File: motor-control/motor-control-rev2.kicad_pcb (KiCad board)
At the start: 2 copper layers, 155.7 x 66 mm, 79 parts, among them P1 CONN_02X12, P2 to_motor_phase_1, P3 to_motor_phase_2, P4 to_motor_phase_3, P5 CONN_01X01, P6 CONN_01X01, P7 CONN_01X04, Q1 csd19505kcs, Q10 csd19505kcs, Q11 csd19505kcs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

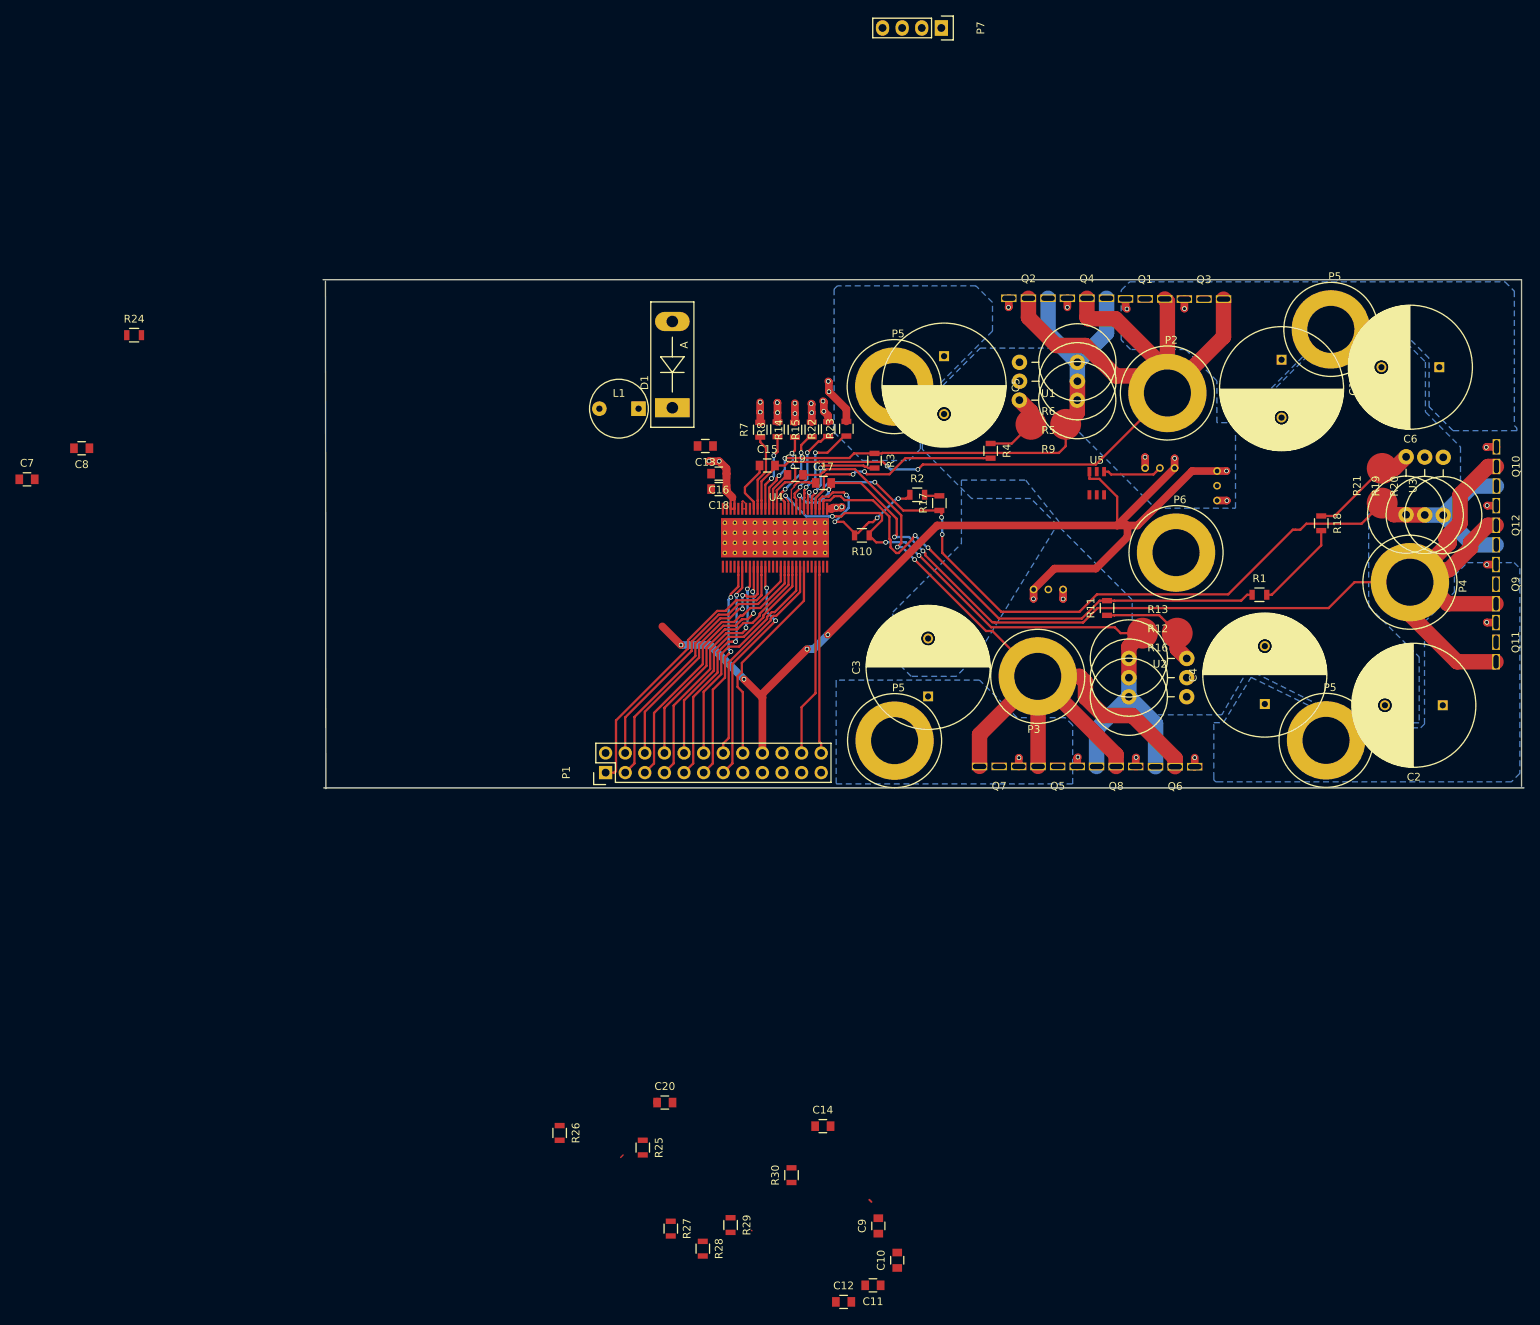
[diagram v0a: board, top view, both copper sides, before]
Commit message: Moved in all components, need last traces and GND
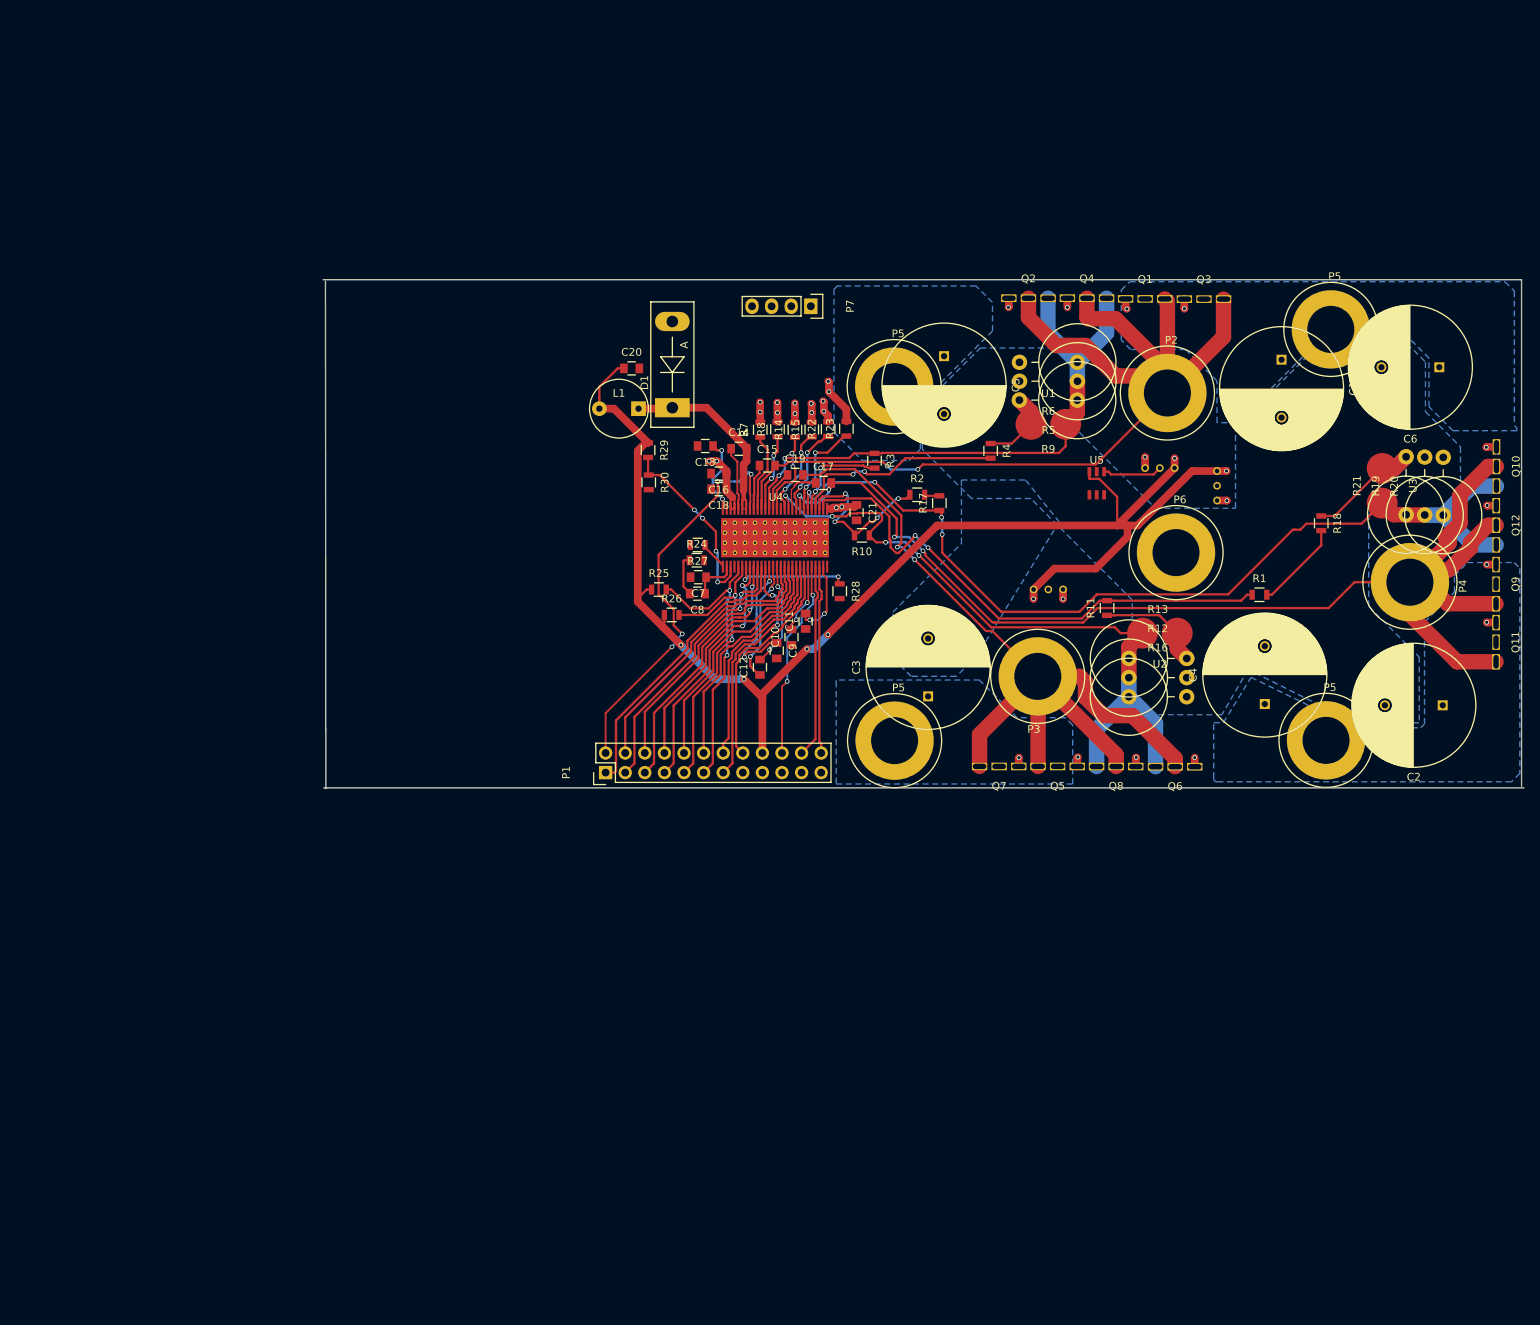
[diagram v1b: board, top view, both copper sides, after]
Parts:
- added C21: C_Small, Capacitors_SMD:C_0805, F.Cu at (110.8, 53.7)
- moved R29 101.0 mm to (83.7, 45.6)
- moved C20 95.2 mm to (81.6, 35.1)
- moved R30 91.7 mm to (83.8, 49.8), turned to 270 degrees
- moved R27 88.7 mm to (90.2, 57.9), turned to 180 degrees
- moved C14 88.5 mm to (95.5, 45.5)
- moved C7 87.9 mm to (90.2, 62.1), turned to 180 degrees
- moved R28 87.0 mm to (108.6, 63.9)
- moved C11 86.5 mm to (104.2, 67.8), turned to 90 degrees
- moved C12 83.0 mm to (98.2, 73.8), turned to 90 degrees
- moved C8 82.0 mm to (90.1, 64.2)
- moved C10 81.9 mm to (102.3, 69.9)
- moved R24 78.5 mm to (90.0, 59.9)
- moved C9 75.7 mm to (100.4, 71.6), turned to 270 degrees
- moved R25 72.4 mm to (85.1, 63.7), turned to 0 degrees
- moved R26 68.7 mm to (86.8, 67.0), turned to 0 degrees
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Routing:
- net /Gate-Driver/VDD_SPI: track 0.00 -> 53.3 mm, vias 0 -> 4
- net VCC: track 135.4 -> 180.6 mm
- net Net-(C14-Pad2): track 2.86 -> 29.7 mm
- net /Gate-Driver/REF: track 0.00 -> 25.9 mm, vias 0 -> 2
- net Net-(R29-Pad2): track 0.00 -> 23.9 mm, vias 0 -> 4
- net Net-(C9-Pad1): track 0.00 -> 18.2 mm, vias 0 -> 2
- net Net-(C12-Pad1): track 0.00 -> 16.0 mm, vias 0 -> 2
- net Net-(R28-Pad1): track 0.00 -> 15.0 mm, vias 0 -> 2
- net Net-(C12-Pad2): track 0.00 -> 13.6 mm, vias 0 -> 2
- net Net-(C13-Pad1): track 0.00 -> 9.96 mm, vias 0 -> 2
- net Net-(C11-Pad2): track 0.00 -> 9.96 mm, vias 0 -> 2
- net /Gate-Driver/nOCTW: track 28.8 -> 38.8 mm
- net Net-(C10-Pad2): track 0.00 -> 9.06 mm, vias 0 -> 2
- net Net-(C14-Pad1): track 0.12 -> 9.02 mm
- net /Gate-Driver/nFault: track 30.4 -> 38.3 mm
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
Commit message: All components in place, now to fix it up
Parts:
- moved P7 56.2 mm to (158.1, 45.0)
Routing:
- net /power mosfets & current sensing/hall_3: track 1.28 -> 76.6 mm, vias 1 -> 5
- net /power mosfets & current sensing/hall_2: track 1.41 -> 72.6 mm, vias 1 -> 4
- net /power mosfets & current sensing/hall_1: track 1.24 -> 51.4 mm, vias 1 -> 5
- net GND: track 45.8 -> 71.8 mm
- net Net-(P7-Pad1): track 0.00 -> 18.0 mm, vias 0 -> 1
- net Net-(P7-Pad2): track 0.00 -> 18.0 mm, vias 0 -> 1
- net Net-(P7-Pad3): track 0.00 -> 17.5 mm, vias 0 -> 1
- net Net-(P7-Pad4): track 0.00 -> 10.3 mm
- net /Gate-Driver/SL_C: track 119.4 -> 118.3 mm
- net VCC: track 180.6 -> 179.6 mm

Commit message: Stuff I didn't commit from last time
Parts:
- moved C6 2.48 mm to (188.8, 35.1)
- moved C1 0.62 mm to (165.2, 33.9)
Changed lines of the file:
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@@
     (links 228)
     (no_connects 38)
-    (area 41.530199 23.483499 197.331401 89.584601)
+    (area 41.530199 20.5104 197.331401 92.527833)
     (thickness 1.6)
     (drawings 5)
@@
       (padsonsilk false)
       (subtractmaskfromsilk false)
-      (outputformat 4)
+      (outputformat 1)
       (mirror false)
-      (drillshape 2)
+      (drillshape 0)
       (scaleselection 1)
       (outputdirectory "C:/Users/terminator/Documents/classwork/senior design/plots/"))
@@
   )
   (module Capacitors_ThroughHole:C_Radial_D16_L30_P7.5 (layer F.Cu)
-    (at 165.8366 33.9274 270)
+    (at 165.2143 33.9344 270)
     (descr "Radial Electrolytic Capacitor Diameter 16mm x Length 25mm, Pitch 7.5mm")
     (tags "Electrolytic Capacitor")
@@
   )
   (module Capacitors_ThroughHole:C_Radial_D16_L30_P7.5 (layer F.Cu)
-    (at 186.2836 34.8996 180)
+    (at 188.7601 35.052 180)
     (descr "Radial Electrolytic Capacitor Diameter 16mm x Length 25mm, Pitch 7.5mm")
     (tags "Electrolytic Capacitor")
@@
     (polygon
       (pts
-        (xy 183.6674 80.9879) (xy 175.3362 80.9879) (xy 161.5059 74.0791) (xy 158.0896 79.9465) (xy 146.4818 79.9465)
+        (xy 182.9689 80.3148) (xy 177.546 79.7941) (xy 161.3662 73.0504) (xy 157.1879 79.502) (xy 146.4818 79.9465)
         (xy 146.4818 65.0621) (xy 133.3373 51.9176) (xy 125.6665 51.9176) (xy 119.2784 45.5295) (xy 119.2784 39.9288)
         (xy 126.7841 32.4231) (xy 138.7475 32.4231) (xy 138.7475 42.4561) (xy 149.4663 53.1749) (xy 159.8676 53.1749)
-        (xy 159.8676 42.7736) (xy 172.5803 30.0609) (xy 180.3273 30.0609) (xy 184.4802 34.2138) (xy 184.4802 40.6781)
-        (xy 189.0268 45.2247) (xy 189.0268 53.9242) (xy 177.1269 53.9242) (xy 177.1269 65.9003) (xy 183.6674 72.4408)
+        (xy 160.5407 42.9006) (xy 168.4909 34.7218) (xy 169.6974 35.6235) (xy 174.6885 35.2171) (xy 177.5968 32.4739)
+        (xy 177.9651 30.1625) (xy 180.8861 30.2006) (xy 184.4802 34.2138) (xy 184.4802 40.6781) (xy 189.0268 45.2247)
+        (xy 189.0268 53.9242) (xy 177.1269 53.9242) (xy 177.1269 65.9003) (xy 183.1213 72.4154)
       )
     )

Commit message: Added bottom solder mask layer
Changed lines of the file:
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@@
-    (polygon
-      (pts
-        (xy 157.0482 88.1507) (xy 157.0482 80.9752) (xy 158.2928 80.9752) (xy 161.8869 75.0951) (xy 169.9133 79.0067)
-        (xy 173.8884 79.0067) (xy 176.5173 81.6356) (xy 183.8706 81.6356) (xy 184.3659 81.1403) (xy 184.3659 67.9323)
-        (xy 188.2394 64.0588) (xy 188.2394 61.8998) (xy 189.9158 60.2234) (xy 195.9864 60.2234) (xy 196.723 60.96)
-        (xy 196.723 87.5411) (xy 195.6308 88.6333) (xy 157.6959 88.6333) (xy 157.3022 88.6333) (xy 157.0482 88.3793)
-      )
-    )
-  )
-  (zone (net 1) (net_name +batt) (layer B.Cu) (hatch edge 0.508)
-    (connect_pads yes (clearance 0.508))
-    (min_thickness 0.254)
-    (fill yes (arc_segments 16) (thermal_gap 0.508) (thermal_bridge_width 0.508))
     (polygon
       (pts
@@
       )
     )
+  )
+  (zone (net 1) (net_name +batt) (layer B.Cu) (hatch edge 0.508)
+    (connect_pads yes (clearance 0.508))
+    (min_thickness 0.254)
+    (fill yes (arc_segments 16) (thermal_gap 0.508) (thermal_bridge_width 0.508))
+    (polygon
+      (pts
+        (xy 156.50718 86.94928) (xy 156.50718 80.3021) (xy 162.56254 74.24674) (xy 166.74084 74.24674) (xy 169.86504 77.37094)
+        (xy 174.1043 77.37094) (xy 178.07178 81.33842) (xy 181.64556 81.33842) (xy 183.47944 79.50454) (xy 183.47944 70.66534)
+        (xy 188.80328 65.3415) (xy 188.80328 62.2681) (xy 190.00724 61.06414) (xy 195.8975 61.06414) (xy 196.40804 61.57468)
+        (xy 196.40804 86.05774) (xy 193.5353 88.93048) (xy 158.4579 88.93048) (xy 156.49956 86.97214)
+      )
+    )
+  )
+  (zone (net 1) (net_name +batt) (layer B.Mask) (hatch edge 0.508)
+    (connect_pads yes (clearance 0.508))
+    (min_thickness 0.254)
+    (fill yes (arc_segments 16) (thermal_gap 0.508) (thermal_bridge_width 0.508))
+    (polygon
+      (pts
+        (xy 183.47944 70.66534) (xy 183.47944 79.44104) (xy 181.62778 81.2927) (xy 178.06924 81.2927) (xy 174.12208 77.34554)
+        (xy 169.88536 77.34554) (xy 166.74846 74.20864) (xy 162.54984 74.20864) (xy 156.47416 80.28432) (xy 156.47416 87.0077)
+        (xy 158.4325 88.96604) (xy 193.53276 88.96604) (xy 196.4436 86.0552) (xy 196.4436 76.7461) (xy 194.27444 74.57694)
+        (xy 192.8241 74.57694) (xy 192.4177 74.17054) (xy 192.4177 69.1261) (xy 191.63538 68.34378) (xy 191.63538 67.564)
+        (xy 192.53962 66.65976) (xy 192.53962 64.5414) (xy 192.96634 64.11468) (xy 194.36588 64.11468) (xy 194.63004 64.37884)
+        (xy 194.63004 74.9046) (xy 196.4436 76.71816) (xy 196.4436 61.56198) (xy 195.88734 61.00572) (xy 195.15836 61.00572)
+        (xy 194.59194 61.57214) (xy 194.59194 61.8109) (xy 192.76314 61.8109) (xy 192.20688 61.25464) (xy 192.01384 61.25464)
+        (xy 189.92596 61.25464) (xy 188.94552 62.23508) (xy 188.94552 65.2907) (xy 183.60898 70.62724) (xy 183.51754 70.62724)
+      )
+    )
+  )
+  (zone (net 1) (net_name +batt) (layer B.Mask) (hatch edge 0.508)
+    (connect_pads yes (clearance 0.508))
+    (min_thickness 0.254)
+    (fill yes (arc_segments 16) (thermal_gap 0.508) (thermal_bridge_width 0.508))
+    (polygon
+      (pts
+        (xy 133.4389 62.23508) (xy 138.19378 62.23508) (xy 147.98294 72.02424) (xy 147.98294 76.7842) (xy 151.15286 79.95412)
+        (xy 155.89504 79.95412) (xy 162.19932 73.64984) (xy 166.85514 73.64984) (xy 170.06316 76.85786) (xy 174.27448 76.85786)
+        (xy 178.23688 80.82026) (xy 181.40426 80.82026) (xy 182.98922 79.2353) (xy 182.98922 70.93712) (xy 180.36032 68.30822)
+        (xy 178.50358 68.30822) (xy 176.12868 65.93332) (xy 176.12868 59.93638) (xy 179.13604 56.92902) (xy 179.13604 52.4891)
+        (xy 180.64734 50.9778) (xy 187.04306 50.9778) (xy 188.99124 49.02962) (xy 188.99124 45.00626) (xy 184.09158 40.1066)
+        (xy 184.09158 33.85312) (xy 180.66512 30.42666) (xy 179.4891 30.42666) (xy 178.78552 31.13024) (xy 178.78552 33.20034)
+        (xy 175.7045 36.28136) (xy 167.28948 36.28136) (xy 160.34766 43.22318) (xy 160.34766 52.54752) (xy 159.42818 53.467)
+        (xy 149.05736 53.467) (xy 137.58926 41.9989) (xy 137.58926 35.02406) (xy 134.42188 31.85668) (xy 127.8509 31.85668)
+        (xy 121.2723 38.43528) (xy 121.2723 39.93134) (xy 119.65178 41.55186) (xy 119.65178 45.76064) (xy 124.5489 50.65776)
+        (xy 124.5489 56.94426) (xy 115.5065 65.98666) (xy 115.5065 72.43318) (xy 117.67058 74.59726) (xy 122.83948 74.59726)
+        (xy 131.953 65.48374) (xy 131.953 62.89802) (xy 132.61594 62.23508)
+      )
+    )
+  )
+  (zone (net 1) (net_name +batt) (layer B.Mask) (hatch edge 0.508)
+    (connect_pads yes (clearance 0.508))
+    (min_thickness 0.254)
+    (fill yes (arc_segments 16) (thermal_gap 0.508) (thermal_bridge_width 0.508))
+    (polygon
+      (pts
+        (xy 108.18114 75.83424) (xy 108.18114 88.64854) (xy 108.27766 88.74506) (xy 123.75642 88.74506) (xy 125.10262 87.39886)
+        (xy 125.10262 85.91042) (xy 125.44552 85.56752) (xy 127.89154 85.56752) (xy 128.2827 85.95868) (xy 128.2827 87.30234)
+        (xy 127.86614 87.7189) (xy 125.42012 87.7189) (xy 125.1077 87.40648) (xy 123.76658 88.7476) (xy 129.18186 88.7476)
+        (xy 130.43916 87.4903) (xy 130.43916 85.73262) (xy 131.47548 84.6963) (xy 132.14096 84.6963) (xy 132.65912 85.21446)
+        (xy 132.65912 85.55482) (xy 135.44042 85.55482) (xy 135.82904 85.94344) (xy 135.82904 87.33536) (xy 135.46836 87.69604)
+        (xy 130.60172 87.69604) (xy 130.41884 87.51316) (xy 129.1844 88.7476) (xy 138.53922 88.7476) (xy 138.72972 88.5571)
+        (xy 138.72972 87.89162) (xy 138.52652 87.68842) (xy 138.12012 87.68842) (xy 137.87628 87.44458) (xy 137.87628 85.8901)
+        (xy 138.19632 85.57006) (xy 138.7094 85.05698) (xy 138.7094 81.28762) (xy 137.77976 80.35798) (xy 135.86968 80.35798)
+        (xy 135.636 80.59166) (xy 131.70916 80.59166) (xy 126.6317 75.5142) (xy 108.50118 75.5142)
+      )
+    )
+  )
+  (zone (net 1) (net_name +batt) (layer B.Mask) (hatch edge 0.508)
+    (connect_pads yes (clearance 0.508))
+    (min_thickness 0.254)
+    (fill yes (arc_segments 16) (thermal_gap 0.508) (thermal_bridge_width 0.508))
+    (polygon
+      (pts
+        (xy 142.9258 86.487) (xy 142.9258 82.23758) (xy 145.7325 79.43088) (xy 146.3548 79.43088) (xy 148.45792 81.534)
+        (xy 148.45792 86.74862) (xy 150.03018 86.74862) (xy 150.5585 86.2203) (xy 150.5585 80.67802) (xy 147.09648 77.216)
+        (xy 147.09648 74.6506) (xy 146.48688 74.041) (xy 145.58772 74.041) (xy 144.97812 74.6506) (xy 144.97812 77.1525)
+        (xy 140.77696 81.35366) (xy 140.77696 86.47938) (xy 142.92834 86.47938) (xy 142.92834 86.47938)
+      )
+    )
+  )
+  (zone (net 1) (net_name +batt) (layer B.Mask) (hatch edge 0.508)
+    (connect_pads yes (clearance 0.508))
+    (min_thickness 0.254)
+    (fill yes (arc_segments 16) (thermal_gap 0.508) (thermal_bridge_width 0.508))
+    (polygon
+      (pts
+        (xy 193.92646 58.98134) (xy 190.1952 58.98134) (xy 186.39536 55.1815) (xy 184.06364 55.1815) (xy 183.36768 54.48554)
+        (xy 183.36768 53.60162) (xy 183.97728 52.99202) (xy 186.33186 52.99202) (xy 190.08852 49.23536) (xy 194.056 49.23536)
+        (xy 194.056 50.90922) (xy 193.59372 51.3715) (xy 191.00292 51.3715) (xy 188.61024 53.76418) (xy 188.61024 54.39918)
+        (xy 191.0715 56.86044) (xy 193.69532 56.86044) (xy 193.69532 58.75274) (xy 193.92392 58.98134)
+      )
+    )
+  )
+  (zone (net 1) (net_name +batt) (layer B.Mask) (hatch edge 0.508)
+    (connect_pads yes (clearance 0.508))
+    (min_thickness 0.254)
+    (fill yes (arc_segments 16) (thermal_gap 0.508) (thermal_bridge_width 0.508))
+    (polygon
+      (pts
+        (xy 167.39616 34.62782) (xy 160.05556 41.96842) (xy 158.0007 41.96842) (xy 157.57652 41.54424) (xy 157.57652 36.58616)
+        (xy 153.43378 32.44342) (xy 146.35734 32.44342) (xy 145.21434 31.30042) (xy 145.21434 29.11348) (xy 147.00758 27.32024)
+        (xy 147.00758 25.32888) (xy 147.00758 25.16378) (xy 146.83232 24.98852) (xy 145.38452 24.98852) (xy 145.22704 24.83104)
+        (xy 146.12366 23.93442) (xy 148.53412 23.93442) (xy 149.60092 25.00122) (xy 149.41296 25.00122) (xy 149.17166 25.24252)
+        (xy 149.17166 26.74112) (xy 149.5425 27.11196) (xy 151.81326 27.11196) (xy 152.87498 28.17368) (xy 153.6065 28.17368)
+        (xy 154.75966 27.02052) (xy 154.75966 25.3238) (xy 154.41422 24.97836) (xy 149.5806 24.97836) (xy 148.53666 23.93442)
+        (xy 156.06268 23.93442) (xy 157.16504 25.03678) (xy 156.79674 25.40508) (xy 156.79674 26.81478) (xy 157.10662 27.12466)
+        (xy 159.49676 27.12466) (xy 159.8803 26.74112) (xy 159.8803 25.42032) (xy 159.45358 24.9936) (xy 157.1244 24.9936)
+        (xy 156.06522 23.93442) (xy 195.1863 23.93442) (xy 196.22516 24.97328) (xy 196.22516 42.5704) (xy 195.59778 43.19778)
+        (xy 188.24702 43.19778) (xy 185.039 39.98976) (xy 185.039 33.67786) (xy 180.91658 29.55544) (xy 172.466 29.55544)
+        (xy 167.39616 34.62528)
+      )
+    )
+  )
+  (zone (net 1) (net_name +batt) (layer B.Mask) (hatch edge 0.508)
+    (connect_pads yes (clearance 0.508))
+    (min_thickness 0.254)
+    (fill yes (arc_segments 16) (thermal_gap 0.508) (thermal_bridge_width 0.508))
+    (polygon
+      (pts
+        (xy 107.93476 24.91232) (xy 107.93476 43.2054) (xy 111.67872 46.94936) (xy 117.49024 46.94936) (xy 118.95582 45.48378)
+        (xy 118.95582 39.53256) (xy 128.27762 30.21076) (xy 128.27762 26.4414) (xy 126.14656 24.31034) (xy 108.53674 24.31034)
+      )
+    )
